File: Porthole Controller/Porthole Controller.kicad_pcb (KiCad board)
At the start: 2 copper layers, 65 x 65 mm, 19 parts, among them J1 STRIP1, J2 STRIP2, J3 STRIP3, J4 STRIP4, J5 INMP441, J6 Conn_02x04_Top_Bottom, J7 - +, J8 Conn_01x04, U1 113991054, U2 SN74AHCT125DR

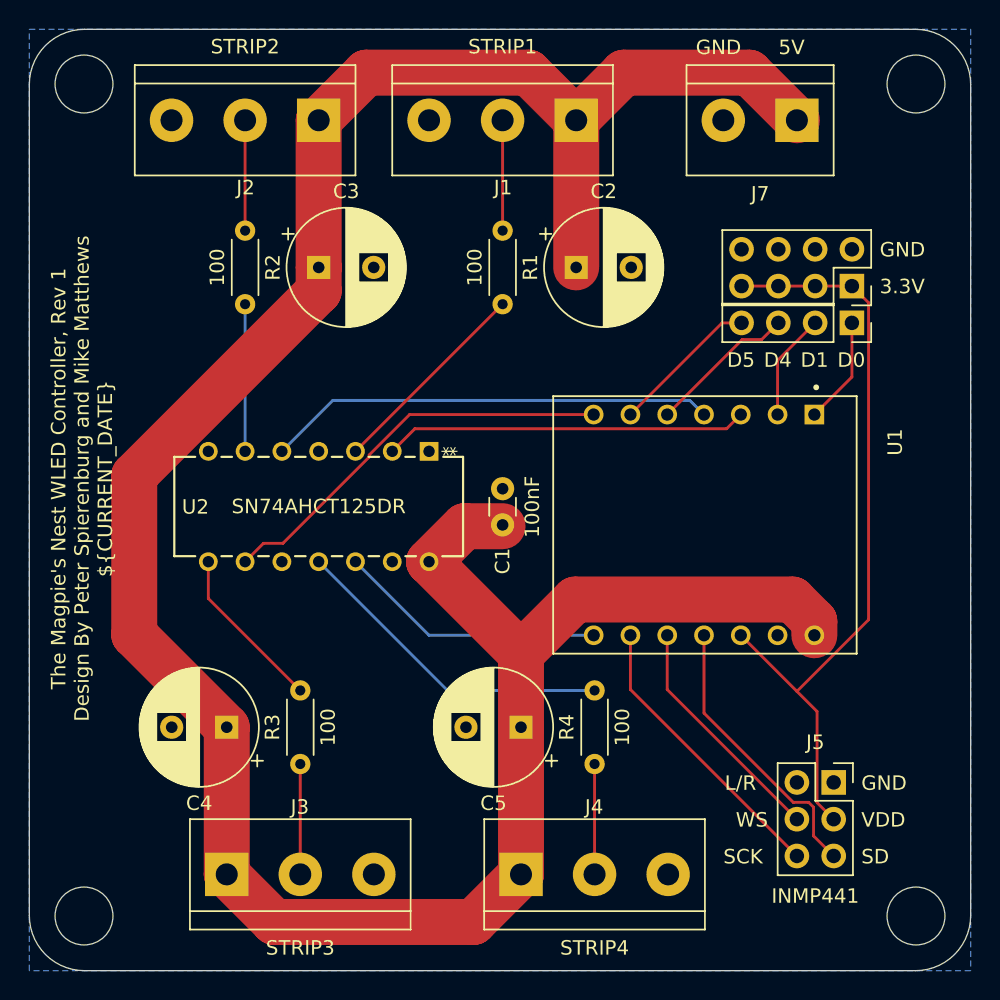
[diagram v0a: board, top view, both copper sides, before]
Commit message: bolden text, fix capacitor labels, reviewed DRC warnings
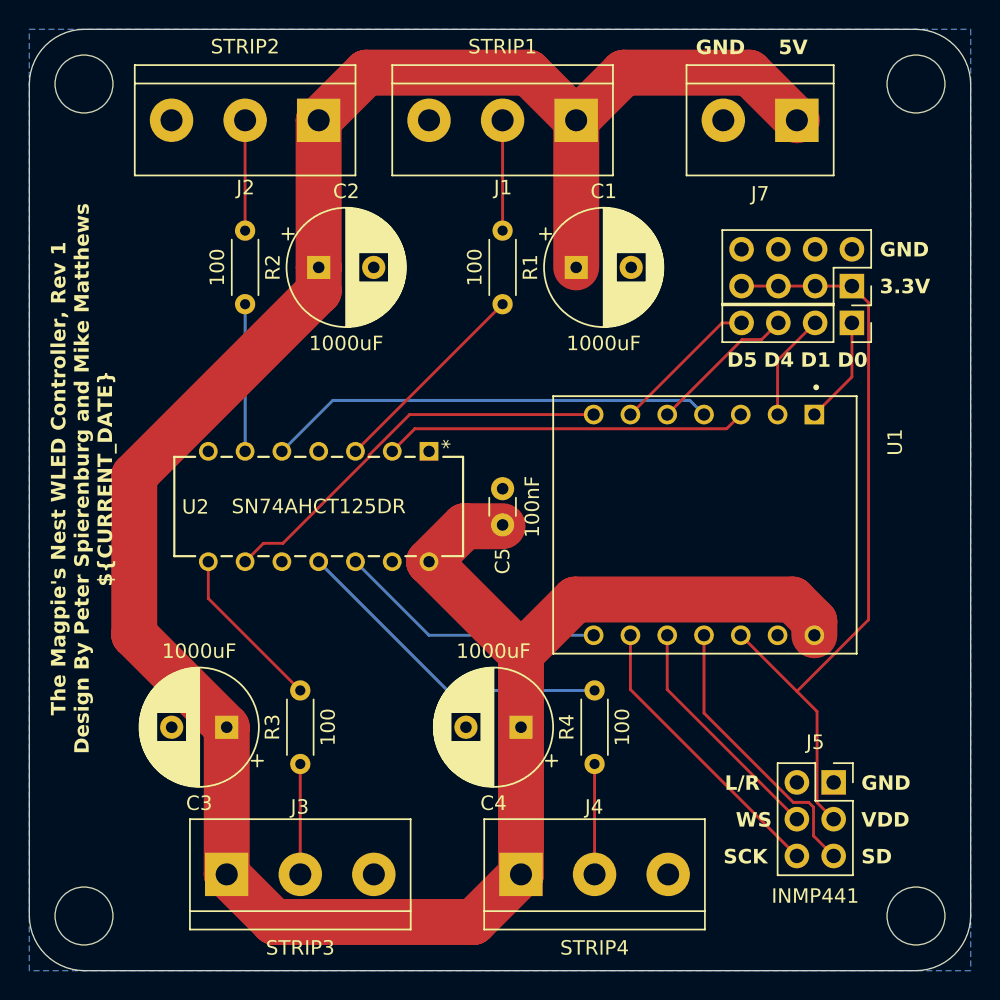
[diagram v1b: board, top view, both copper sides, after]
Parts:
- renumbered C2 to C1, C3 to C2, C4 to C3, C5 to C4, C1 to C5
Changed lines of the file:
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@@
 		(descr "CP, Radial series, Radial, pin pitch=3.80mm, , diameter=8mm, Electrolytic Capacitor")
 		(tags "CP Radial series Radial pin pitch 3.80mm  diameter 8mm Electrolytic Capacitor")
-		(property "Reference" "C2"
+		(property "Reference" "C1"
 			(at 1.9 -5.25 0)
 			(layer "F.SilkS")
@@
 		(property "Value" "1000uF"
 			(at 1.9 5.25 0)
-			(layer "F.Fab")
+			(layer "F.SilkS")
 			(effects
 				(font
@@
 		(descr "CP, Radial series, Radial, pin pitch=3.80mm, , diameter=8mm, Electrolytic Capacitor")
 		(tags "CP Radial series Radial pin pitch 3.80mm  diameter 8mm Electrolytic Capacitor")
-		(property "Reference" "C3"
+		(property "Reference" "C2"
 			(at 1.9 -5.25 0)
 			(layer "F.SilkS")
@@
 		(property "Value" "1000uF"
 			(at 1.9 5.25 0)
-			(layer "F.Fab")
+			(layer "F.SilkS")
 			(effects
 				(font
@@
 		(descr "CP, Radial series, Radial, pin pitch=3.80mm, , diameter=8mm, Electrolytic Capacitor")
 		(tags "CP Radial series Radial pin pitch 3.80mm  diameter 8mm Electrolytic Capacitor")
-		(property "Reference" "C5"
+		(property "Reference" "C4"
 			(at 1.9 -5.25 180)
 			(layer "F.SilkS")
@@
 		(property "Value" "1000uF"
 			(at 1.9 5.25 180)
-			(layer "F.Fab")
+			(layer "F.SilkS")
 			(effects
 				(font
@@
 		)
 		(fp_text user "*"
-			(at 0 -1.4097 90)
+			(at -0.5 -1.4097 90)
 			(layer "F.SilkS")
 			(effects
@@
 		)
 		(fp_text user "*"
-			(at 0 -1.4097 -90)
-			(unlocked yes)
-			(layer "F.SilkS")
-			(effects
-				(font
-					(size 1 1)
-					(thickness 0.15)
-				)
-			)
-		)
-		(fp_text user "*"
-			(at 0.762 0 90)
-			(layer "F.Fab")
-			(effects
-				(font
-					(size 1 1)
-					(thickness 0.15)
-				)
-			)
-		)
-		(fp_text user "*"
-			(at 0.762 0 -90)
+			(at 1 0 -90)
 			(unlocked yes)
 			(layer "F.Fab")
@@
 		(descr "C, Disc series, Radial, pin pitch=2.50mm, , diameter*width=3.0*1.6mm^2, Capacitor, http://www.vishay.com/docs/45233/krseries.pdf")
 		(tags "C Disc series Radial pin pitch 2.50mm  diameter 3.0mm width 1.6mm Capacitor")
-		(property "Reference" "C1"
+		(property "Reference" "C5"
 			(at -2.5 0 -90)
 			(layer "F.SilkS")
@@
 		(descr "CP, Radial series, Radial, pin pitch=3.80mm, , diameter=8mm, Electrolytic Capacitor")
 		(tags "CP Radial series Radial pin pitch 3.80mm  diameter 8mm Electrolytic Capacitor")
-		(property "Reference" "C4"
+		(property "Reference" "C3"
 			(at 1.9 -5.25 180)
 			(layer "F.SilkS")
@@
 		(property "Value" "1000uF"
 			(at 1.9 5.25 180)
-			(layer "F.Fab")
+			(layer "F.SilkS")
 			(effects
 				(font
@@
 			(font
 				(size 1 1)
-				(thickness 0.1)
+				(thickness 0.2)
+				(bold yes)
 			)
 			(justify left bottom)
@@
 			(font
 				(size 1 1)
-				(thickness 0.1)
+				(thickness 0.2)
+				(bold yes)
 			)
 			(justify left bottom)
@@
 			(font
 				(size 1 1)
-				(thickness 0.1)
+				(thickness 0.2)
+				(bold yes)
 			)
 			(justify left bottom)
@@
 			(font
 				(size 1 1)
-				(thickness 0.1)
+				(thickness 0.2)
+				(bold yes)
 			)
 			(justify left bottom)
@@
 			(font
 				(size 1 1)
-				(thickness 0.1)
+				(thickness 0.2)
+				(bold yes)
 			)
 			(justify left bottom)
@@
 			(font
 				(size 1 1)
-				(thickness 0.1)
+				(thickness 0.2)
+				(bold yes)
 			)
 			(justify left bottom)
@@
 			(font
 				(size 1 1)
-				(thickness 0.1)
+				(thickness 0.2)
+				(bold yes)
 			)
 			(justify left bottom)
@@
 			(font
 				(size 1 1)
-				(thickness 0.1)
+				(thickness 0.2)
+				(bold yes)
 			)
 			(justify left bottom)
@@
 			(font
 				(size 1 1)
-				(thickness 0.1)
+				(thickness 0.2)
+				(bold yes)
 			)
 			(justify left bottom)
@@
 			(font
 				(size 1 1)
-				(thickness 0.1)
+				(thickness 0.2)
+				(bold yes)
 			)
 			(justify left bottom)
@@
 			(font
 				(size 1 1)
-				(thickness 0.1)
+				(thickness 0.2)
+				(bold yes)
 			)
 			(justify bottom)
@@
 			(font
 				(size 1 1)
-				(thickness 0.1)
+				(thickness 0.2)
+				(bold yes)
 			)
 			(justify left bottom)
@@
 			(font
 				(size 1 1)
-				(thickness 0.1)
+				(thickness 0.2)
+				(bold yes)
 			)
 			(justify left bottom)
@@
 			(font
 				(size 1 1)
-				(thickness 0.1)
+				(thickness 0.2)
+				(bold yes)
 			)
 			(justify left bottom)
@@
 			(font
 				(size 1 1)
-				(thickness 0.1)
+				(thickness 0.2)
+				(bold yes)
 			)
 			(justify left bottom)
@@
 			(font
 				(size 1 1)
-				(thickness 0.1)
+				(thickness 0.2)
+				(bold yes)
 			)
 			(justify left top mirror)
@@
 		)
 		(height -8.31)
-		(gr_text "2559.0551 mils"
+		(gr_text "2.5591 in"
 			(at 170 69.35 0)
 			(layer "User.2")
@@
 		)
 		(height 7.31)
-		(gr_text "2559.0551 mils"
+		(gr_text "2.5591 in"
 			(at 132.85 107.5 90)
 			(layer "User.2")
